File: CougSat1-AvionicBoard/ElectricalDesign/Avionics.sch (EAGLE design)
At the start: 186 parts, among them J11 -Y, J12 +Z, J13 +X, J14 -Z, J15 +Y, J3 SWD, J4 CougSat Card, J5 -X, J8 SWD, J9 SWD, U1 STM32L476RGT, U10 BNO055, U11 128KB, U12 TXS0102DQM, U13 TXS0102DQM, U14 LTC2499, U15 BNO055, U16 BNO055, U17 TXS0102DQM, U18 TXS0102DQM, U19 INA199C1, U2 STM32L476RGT, U20 INA199C1, U21 INA199C1, U3 STM32L476RGT, U4 128KB, U5 DRV8837, U6 DRV8837, U7 DRV8837, U8 LTC2499, U9 Venus838FLPx-L, Y1 16MHz ±10ppm, Y10 16MHz ±10ppm, Y2 32.768kHz ±10ppm, Y3 16MHz ±10ppm, Y4 32.768kHz ±10ppm, Y6 32.768kHz ±10ppm, Y7 32.768kHz ±10ppm, Y8 32.768kHz ±10ppm, Y9 32.768kHz ±10ppm

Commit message: Updated ADCs
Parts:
- removed R14, R15, R29, R30: 20kΩ 0.1%, CougsInSpace-Resistors:RES-V-PAIRED-20K-1616
- removed R16, R17, R31: 20kΩ 0.1%, CougsInSpace-Resistors:RES-H-PAIRED-20K-1616
- removed RT11: 68kΩ 5%, CougsInSpace-Resistors:THERMISTOR-H-68K-1608
- added C20, C21, C50, C52, C53, C65, C66, C67, C68, C70, C71: 100nF 10%, CougsInSpace-Capacitors:CAP-V-100NF-1608
- added C51, C69: 1µF 10%, CougsInSpace-Capacitors:CAP-V-1UF-1608
- added C64: 10µF 10%, CougsInSpace-Capacitors:CAP-V-10UF-1608
- added R64, R65, R66, R67: 20kΩ 0.1%, CougsInSpace-Resistors:RES-V-PAIRED-20K-1616
- added R68, R69, R70, RN1: 20kΩ 0.1%, CougsInSpace-Resistors:RES-H-PAIRED-20K-1616
- added U22, U23: LTC2499, CougsInSpace-IC-Conversion:LTC2499
- added U24, U29: AD8515, CougsInSpace-IC-Amplifiers:OPAMP-1-AD8515
- added U25, U26: AD7291, CougsInSpace-IC-Conversion:AD7291
- C34: value 100nF 10% -> 10µF 10%; device CougsInSpace-Capacitors:CAP-V-100NF-1608 -> CougsInSpace-Capacitors:CAP-V-10UF-1608
- C44: value 100nF 10% -> 1µF 10%; device CougsInSpace-Capacitors:CAP-V-100NF-1608 -> CougsInSpace-Capacitors:CAP-V-1UF-1608
- U14: value LTC2499 -> AD8515; device CougsInSpace-IC-Conversion:LTC2499 -> CougsInSpace-IC-Amplifiers:OPAMP-1-AD8515
- U8: value LTC2499 -> AD7291; device CougsInSpace-IC-Conversion:LTC2499 -> CougsInSpace-IC-Conversion:AD7291
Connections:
- removed net ADC_COIL-X_COIL+: R16.A2, U8.CH1
- removed net ADC_COIL-X_OUT1: R16.B2, U8.CH0
- removed net ADC_COIL-Y_COIL+: R17.A2, U8.CH3
- removed net ADC_COIL-Y_OUT1: R17.B2, U8.CH2
- removed net ADC_COIL-Z_COIL+: R31.A2, U8.CH5
- removed net ADC_COIL-Z_OUT1: R31.B2, U8.CH4
- removed net N$25: R14.A2, U8.MUXOUTP
- removed net N$28: R29.A2, U14.MUXOUTP
- removed net N$51: R29.B1, R30.B2, U14.ADCINN
- removed net N$65: R29.A1, R30.A2, U14.ADCINP
- new net ADCS_HALF_REF: C44.1, C50.1, U24.IN-, U24.OUT
- new net ADC_COIL-X_COIL+1: R68.A2, U22.CH1
- new net ADC_COIL-X_OUT2: R68.B2, U22.CH0
- new net ADC_COIL-Y_COIL+1: R69.A2, U22.CH3
- new net ADC_COIL-Y_OUT2: R69.B2, U22.CH2
- new net ADC_COIL-Z_COIL+1: R70.A2, U22.CH5
- new net ADC_COIL-Z_OUT2: R70.B2, U22.CH4
- new net AVREF-0: C51.1, C52.1, R47.2, R48.2, R49.2, R50.2, R51.2, R52.2, R53.2, R54.2, U14.IN-, U14.OUT
- new net AVREF-1: R55.2, R56.2, R57.2, R58.2, R59.2, R60.2
- new net N$32: R64.B1, R65.B2, U23.ADCINN
- new net N$33: R64.A1, R65.A2, U23.ADCINP
- new net N$34: R64.B2, U23.MUXOUTN
- new net N$39: R64.A2, U23.MUXOUTP
- new net N$40: R66.B1, R67.B2, U22.ADCINN
- new net N$41: R66.A1, R67.A2, U22.ADCINP
- new net N$42: R66.B2, U22.MUXOUTN
- new net N$43: R66.A2, U22.MUXOUTP
- net 3.3V_0: now also U23.CA0, U23.VCC, U26.AS1, U26.VDRIVE; no longer U14.CA0, U14.VCC
- net 3.3V_2: now also U22.VCC, U25.AS1, U25.VDRIVE, U8.AS0, U8.AS1, U8.VDRIVE; no longer U8.VCC
- net 3.3V_6: now also C20.1, C21.1, C53.1, C65.1, C66.1, C67.1, C68.1, C71.1; no longer C34.1, C44.1
- net ADCS_I2C0_SCL: now also U22.SCL, U25.SCL
- net ADCS_I2C0_SDA: now also U22.SDA, U25.SDA
- net AGND: now also C34.2, C44.2, C50.2, C51.2, C52.2, C64.2, C69.2, C70.2, R65.A1, R65.B1, R67.A1, R67.B1, RN1.A2, U14.V-, U22.COM, U22.REF-, U23.COM, U23.REF-, U24.V-, U25.AGND, U26.AGND, U29.V-, U8.AGND; no longer R15.A1, R15.B1, R30.A1, R30.B1, U14.COM, U14.REF-, U8.COM, U8.REF-
- net AVDD: now also U14.V+, U22.REF+, U23.REF+, U24.V+, U25.VDD, U26.VDD, U29.V+, U8.VDD; no longer RT11.2, U14.REF+, U8.REF+
- net AVREF: now also U22.CH8, U23.CH8; no longer R47.2, R48.2, R49.2, R50.2, R51.2, R52.2, R53.2, R54.2, R55.2, R56.2, R57.2, R58.2, R59.2, R60.2, U14.CH8, U8.CH8
- net BUS_I2C0_SCL: now also U26.SCL
- net BUS_I2C0_SDA: now also U26.SDA
- net COIL-X_COIL+: now also R68.A1; no longer R16.A1
- net COIL-X_CURRENT: now also U8.IN0
- net COIL-X_OUT1: now also R68.B1; no longer R16.B1
- net COIL-Y_COIL+: now also R69.A1; no longer R17.A1
- net COIL-Y_CURRENT: now also U8.IN1
- net COIL-Y_OUT1: now also R69.B1; no longer R17.B1
- net COIL-Z_COIL+: now also R70.A1; no longer R31.A1
- net COIL-Z_CURRENT: now also U8.IN2
- net COIL-Z_OUT1: now also R70.B1; no longer R31.B1
- net DGND: now also C20.2, C21.2, C53.2, C65.2, C66.2, C67.2, C68.2, C71.2, U22.CA0, U22.CA1, U22.CA2, U22.DGND, U22.F0, U23.CA1, U23.CA2, U23.DGND, U23.F0, U25.DGND, U26.AS0, U26.DGND; no longer C34.2, C44.2, U14.CA1, U14.CA2, U14.DGND, U14.F0, U8.CA0, U8.CA1, U8.CA2, U8.F0
- net N$18: now also C34.1, RN1.B2, U14.IN+, U8.VREF; no longer R14.B1, R15.B2, U8.ADCINN
- net N$19: now also RN1.A1, RN1.B1, U24.IN+; no longer R14.A1, R15.A2, U8.ADCINP
- net N$24: now also C64.1, U26.VREF, U29.IN+; no longer R14.B2, U8.MUXOUTN
- net N$27: now also C69.1, C70.1, U29.IN-, U29.OUT; no longer R29.B2, U14.MUXOUTN
- net TEMP_ADCS: now also U22.CH11, U8.IN7; no longer RT11.1, U8.CH11
- net TEMP_GPS: now also U22.CH6, U8.IN3; no longer U8.CH6
- net TEMP_H-BRIDGE-X: now also U22.CH13, U25.IN0; no longer R59.1, R60.1, RT6.2, RT7.2, U8.CH13
- net TEMP_H-BRIDGE-Y: now also U22.CH14, U25.IN1; no longer U8.CH14
- net TEMP_H-BRIDGE-Z: now also U22.CH15, U25.IN2; no longer U8.CH15
- net TEMP_IFJR: now also U23.CH1, U26.IN1; no longer U14.CH1
- net TEMP_IHU: now also U23.CH0, U26.IN0; no longer U14.CH0
- net TEMP_IMU0: now also U22.CH7, U8.IN4; no longer U8.CH7
- net TEMP_IMU1: now also U22.CH9, U8.IN5; no longer U8.CH9
- net TEMP_IMU2: now also U22.CH10, U8.IN6; no longer U8.CH10
- net TEMP_SD_IFJR0: now also U23.CH4, U26.IN4; no longer U14.CH4
- net TEMP_SD_IFJR1: now also U23.CH5, U26.IN5; no longer U14.CH5
- net TEMP_SD_IHU0: now also R59.1, RT6.2, U23.CH2, U26.IN2; no longer U14.CH2
- net TEMP_SD_IHU1: now also R60.1, RT7.2, U23.CH3, U26.IN3; no longer U14.CH3

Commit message: Adjusted SPI and LED pins
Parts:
- removed C20, C21: 100nF 10%, CougsInSpace-Capacitors:CAP-V-100NF-1608
- removed R64, R65, R66, R67: 20kΩ 0.1%, CougsInSpace-Resistors:RES-V-PAIRED-20K-1616
- removed R68, R69, R70: 20kΩ 0.1%, CougsInSpace-Resistors:RES-H-PAIRED-20K-1616
- removed U22, U23: LTC2499, CougsInSpace-IC-Conversion:LTC2499
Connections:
- removed net ADC_COIL-X_COIL+1: R68.A2, U22.CH1
- removed net ADC_COIL-X_OUT2: R68.B2, U22.CH0
- removed net ADC_COIL-Y_COIL+1: R69.A2, U22.CH3
- removed net ADC_COIL-Y_OUT2: R69.B2, U22.CH2
- removed net ADC_COIL-Z_COIL+1: R70.A2, U22.CH5
- removed net ADC_COIL-Z_OUT2: R70.B2, U22.CH4
- removed net AVREF: U22.CH8, U23.CH8
- removed net N$27: C69.1, C70.1, U29.IN-, U29.OUT
- removed net N$32: R64.B1, R65.B2, U23.ADCINN
- removed net N$33: R64.A1, R65.A2, U23.ADCINP
- removed net N$34: R64.B2, U23.MUXOUTN
- removed net N$39: R64.A2, U23.MUXOUTP
- removed net N$40: R66.B1, R67.B2, U22.ADCINN
- removed net N$41: R66.A1, R67.A2, U22.ADCINP
- removed net N$42: R66.B2, U22.MUXOUTN
- removed net N$43: R66.A2, U22.MUXOUTP
- new net ADCS_LED: DS2.A, U2A.PA5
- net 3.3V_0: no longer U23.CA0, U23.VCC
- net 3.3V_2: no longer U22.VCC
- net 3.3V_6: no longer C20.1, C21.1
- net ADCS_I2C0_SCL: no longer U22.SCL
- net ADCS_I2C0_SDA: no longer U22.SDA
- net AGND: no longer R65.A1, R65.B1, R67.A1, R67.B1, U22.COM, U22.REF-, U23.COM, U23.REF-
- net AVDD: no longer U22.REF+, U23.REF+
- net AVREF-1: now also C69.1, C70.1, U29.IN-, U29.OUT
- net COIL-X_COIL+: no longer R68.A1
- net COIL-X_OUT1: no longer R68.B1
- net COIL-Y_COIL+: no longer R69.A1
- net COIL-Y_OUT1: no longer R69.B1
- net COIL-Z_COIL+: no longer R70.A1
- net COIL-Z_OUT1: no longer R70.B1
- net DGND: no longer C20.2, C21.2, U22.CA0, U22.CA1, U22.CA2, U22.DGND, U22.F0, U23.CA1, U23.CA2, U23.DGND, U23.F0
- net IFJR_LED: now also U1A.PA5; no longer U1A.PA4
- net IFJR_SPI0_MISO: now also U1C.PC4; no longer U1A.PA6
- net IFJR_SPI0_MOSI: now also U1C.PC5; no longer U1A.PA7
- net IFJR_SPI0_SCK: now also U1B.PB10; no longer U1A.PA5
- net IHU_LED: no longer DS2.A, U2A.PA5
- net JTAG_EN_ADCS: now also U1C.PC2; no longer U1C.PC3
- net JTAG_EN_IHU: now also U1C.PC3; no longer U1C.PC4
- net TEMP_ADCS: no longer U22.CH11
- net TEMP_GPS: no longer U22.CH6
- net TEMP_H-BRIDGE-X: no longer U22.CH13
- net TEMP_H-BRIDGE-Y: no longer U22.CH14
- net TEMP_H-BRIDGE-Z: no longer U22.CH15
- net TEMP_IFJR: no longer U23.CH1
- net TEMP_IHU: no longer U23.CH0
- net TEMP_IMU0: no longer U22.CH7
- net TEMP_IMU1: no longer U22.CH9
- net TEMP_IMU2: no longer U22.CH10
- net TEMP_SD_IFJR0: no longer U23.CH4
- net TEMP_SD_IFJR1: no longer U23.CH5
- net TEMP_SD_IHU0: no longer U23.CH2
- net TEMP_SD_IHU1: no longer U23.CH3
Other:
- note added: "8B4>"
- note added: "9C3>"
- note removed: "4A5>"
- note removed: "5A4>"
- note removed: "5B4>"
- note removed: "5C4>"
- note removed: "8A5>"
- note removed: "8C3>"
- note removed: "8D3>"
- note removed: "9A5>"
- note removed: "9C4>"
- note removed: "9D4>"
- note removed: "<3A6"
- note removed: "<4A5"
- note removed: "<4A6"
- note removed: "<5A6"
- note removed: "<5B6"
- note removed: "<5C6"

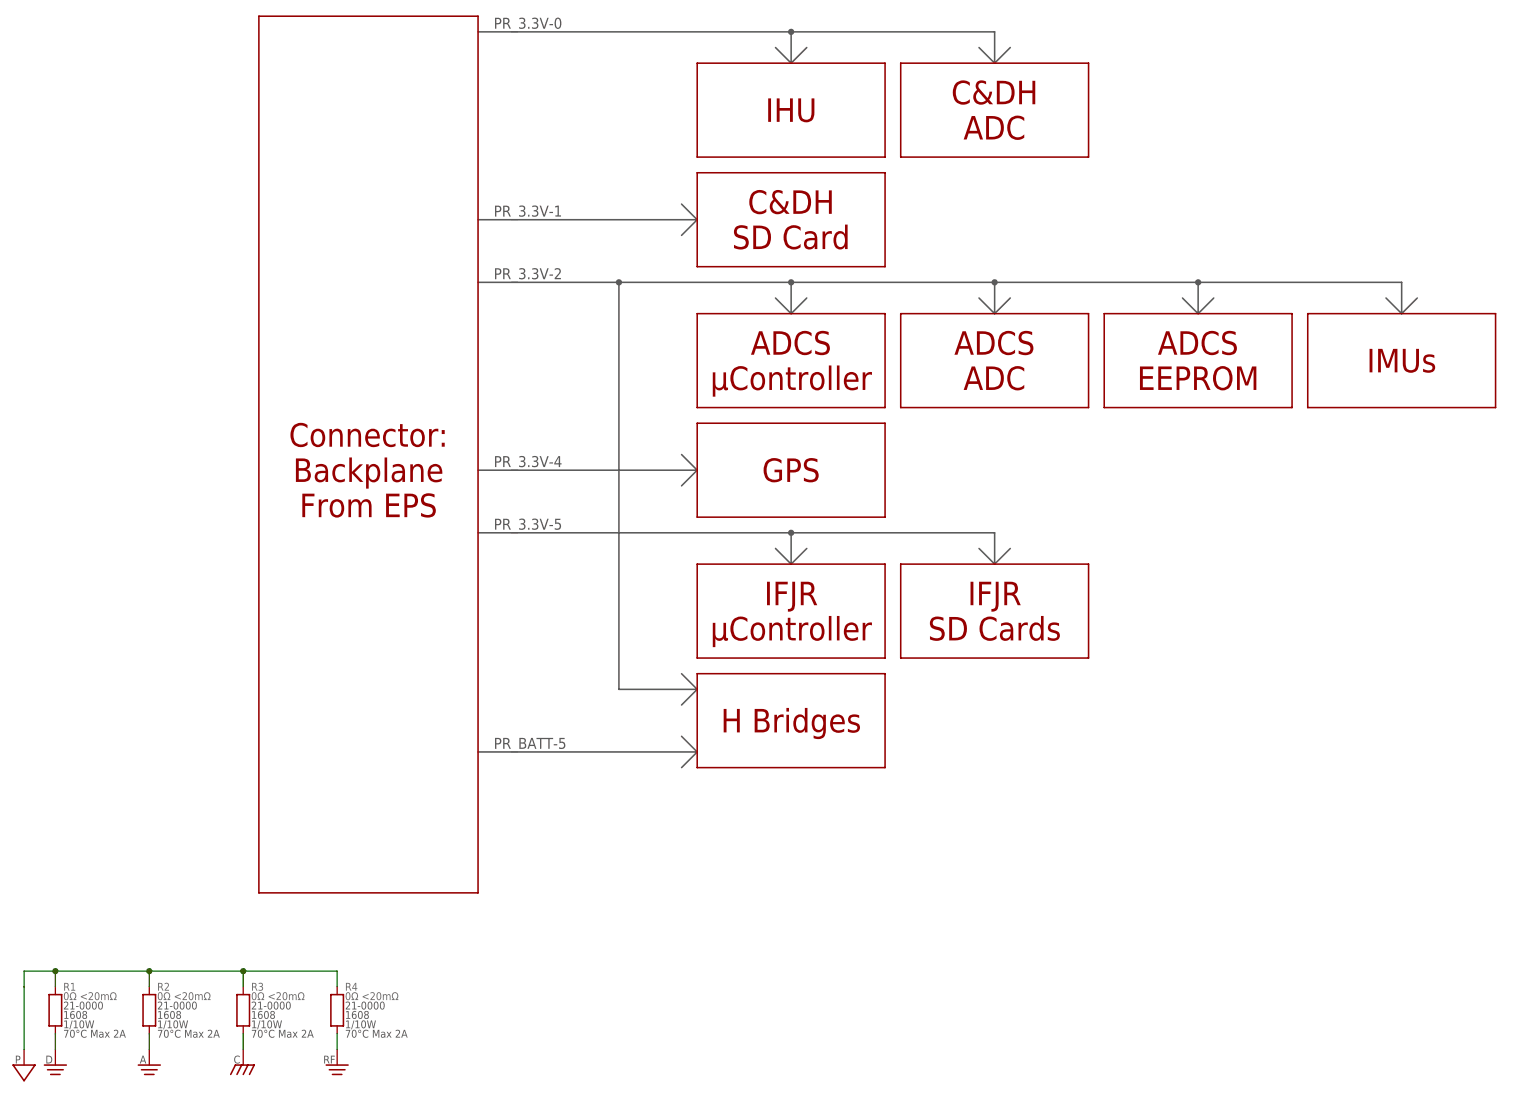
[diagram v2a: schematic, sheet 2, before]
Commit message: Updated Power Rails
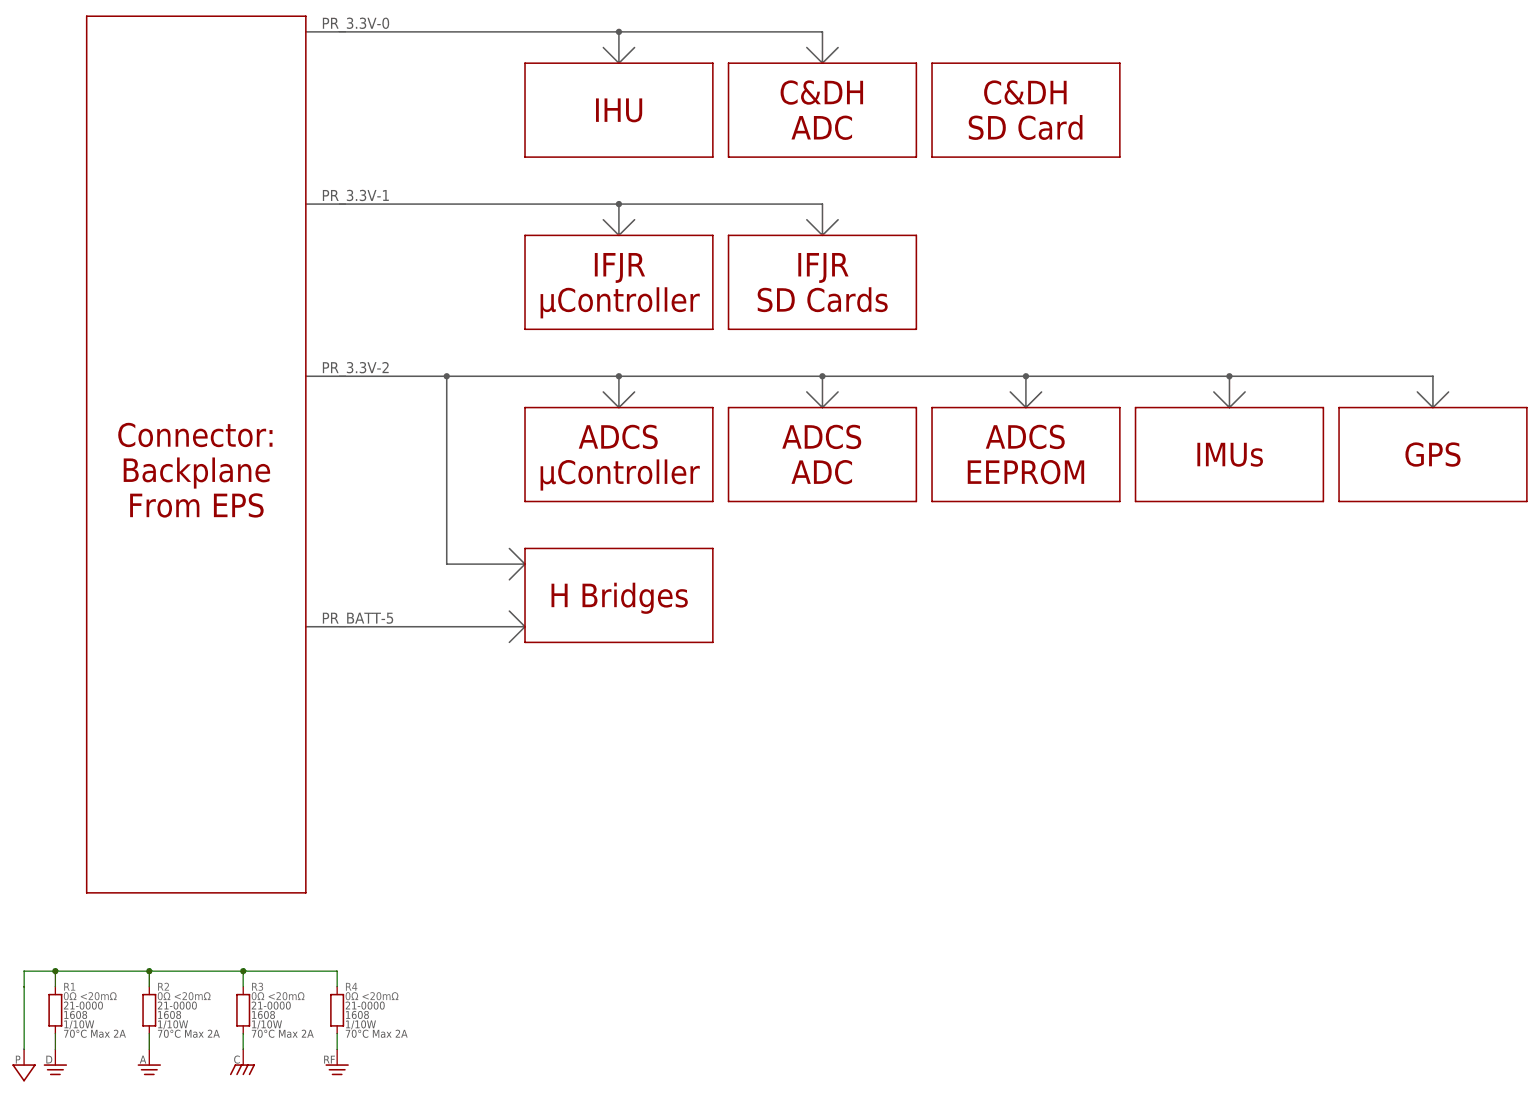
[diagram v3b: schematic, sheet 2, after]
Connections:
- removed net 3.3V_3: C33.1, C35.1, C39.1, C40.1, C41.1, C45.1, C5.1, C6.1, C8.1, R20.2, R32.2, R39.2, R40.2, R41.1, R43.2, U10.VDD, U10.VDDIO, U15.VDD, U15.VDDIO, U16.VDD, U16.VDDIO
- removed net 3.3V_4: C11.1, C12.1, D1.A, DS1.A, J4POWER.PR_3.3V-4, L1.2, R12.2, U9BASE.BOOT, U9BASE.VCC@1, U9BASE.VCC@2
- removed net 3.3V_5: C54.1, C55.1, C56.1, C57.1, J10.VDD, J16.VDD, J2.VDD, J4POWER.PR_3.3V-5, J6.VDD, R25.2, R34.2, R37.2, R44.2, U12.VCCB, U13.VCCB, U17.VCCB, U18.VCCB, U1BASE.VBAT, U1BASE.VDD@1, U1BASE.VDD@2, U1BASE.VDD@3, U1BASE.VDDUSB
- net 3.3V_0: now also J2.VDD, J6.VDD, R25.2, R44.2, U17.VCCA, U18.VCCA
- net 3.3V_1: now also C30.1, C31.1, C54.1, C55.1, C56.1, C57.1, J10.VDD, J16.VDD, R34.2, R37.2, U12.VCCB, U13.VCCB, U17.VCCB, U18.VCCB, U1BASE.VBAT, U1BASE.VDD@1, U1BASE.VDD@2, U1BASE.VDD@3, U1BASE.VDDUSB
- net 3.3V_2: now also C11.1, C12.1, C29.1, C33.1, C35.1, C39.1, C40.1, C41.1, C45.1, C5.1, C53.1, C6.1, C66.1, C67.1, C68.1, C7.1, C71.1, C8.1, D1.A, DS1.A, L1.2, R12.2, R20.2, R32.2, R39.2, R40.2, R41.1, R43.2, U10.VDD, U10.VDDIO, U15.VDD, U15.VDDIO, U16.VDD, U16.VDDIO, U9BASE.BOOT, U9BASE.VCC@1, U9BASE.VCC@2; no longer U17.VCCA, U18.VCCA
- net 3.3V_6: no longer C25.1, C26.1, C29.1, C30.1, C31.1, C53.1, C66.1, C67.1, C68.1, C7.1, C71.1
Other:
- note removed: "PR_3.3V-4"
- note removed: "PR_3.3V-5"
